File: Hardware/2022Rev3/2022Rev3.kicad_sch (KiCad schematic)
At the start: 88 parts, among them J1 Conn_01x04, J2 Conn_01x06, J3 RJ45_LED_Shielded, J4 Conn_01x09, J5 Conn_01x09, Q1 Q_NMOS_DGS, SW1 SW_SPDT, U1 ACS758xCB-200B-PFF, U10 PESD4USB3U-TBS, U11 PESD4USB3U-TBS, U2 LT1910, U3 TRS12433, U4 TRS12450, U5 Teensy4.1_DEV-16771, U6 Opamp_Dual, U7 Opamp_Dual, U8 Opamp_Dual, U9 Opamp_Dual

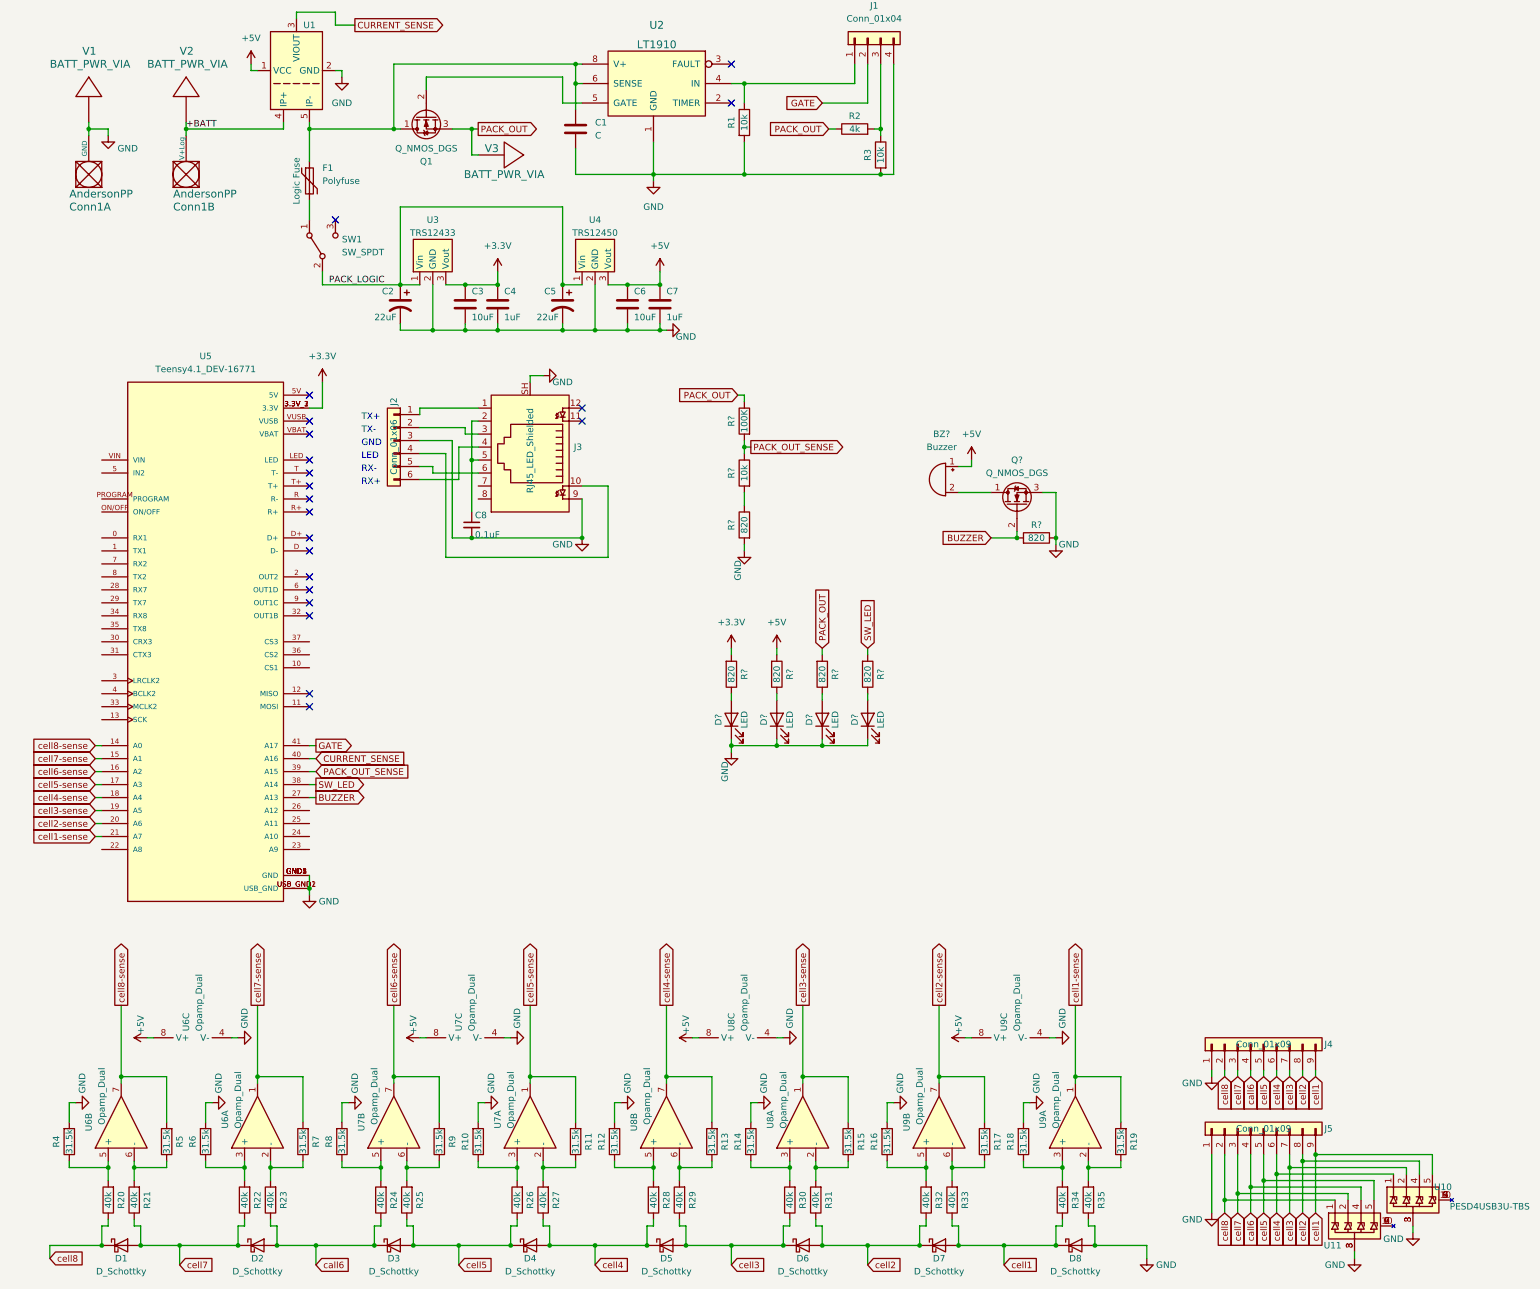
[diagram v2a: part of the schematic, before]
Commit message: BMS layout complete pending ethernet circuit and review
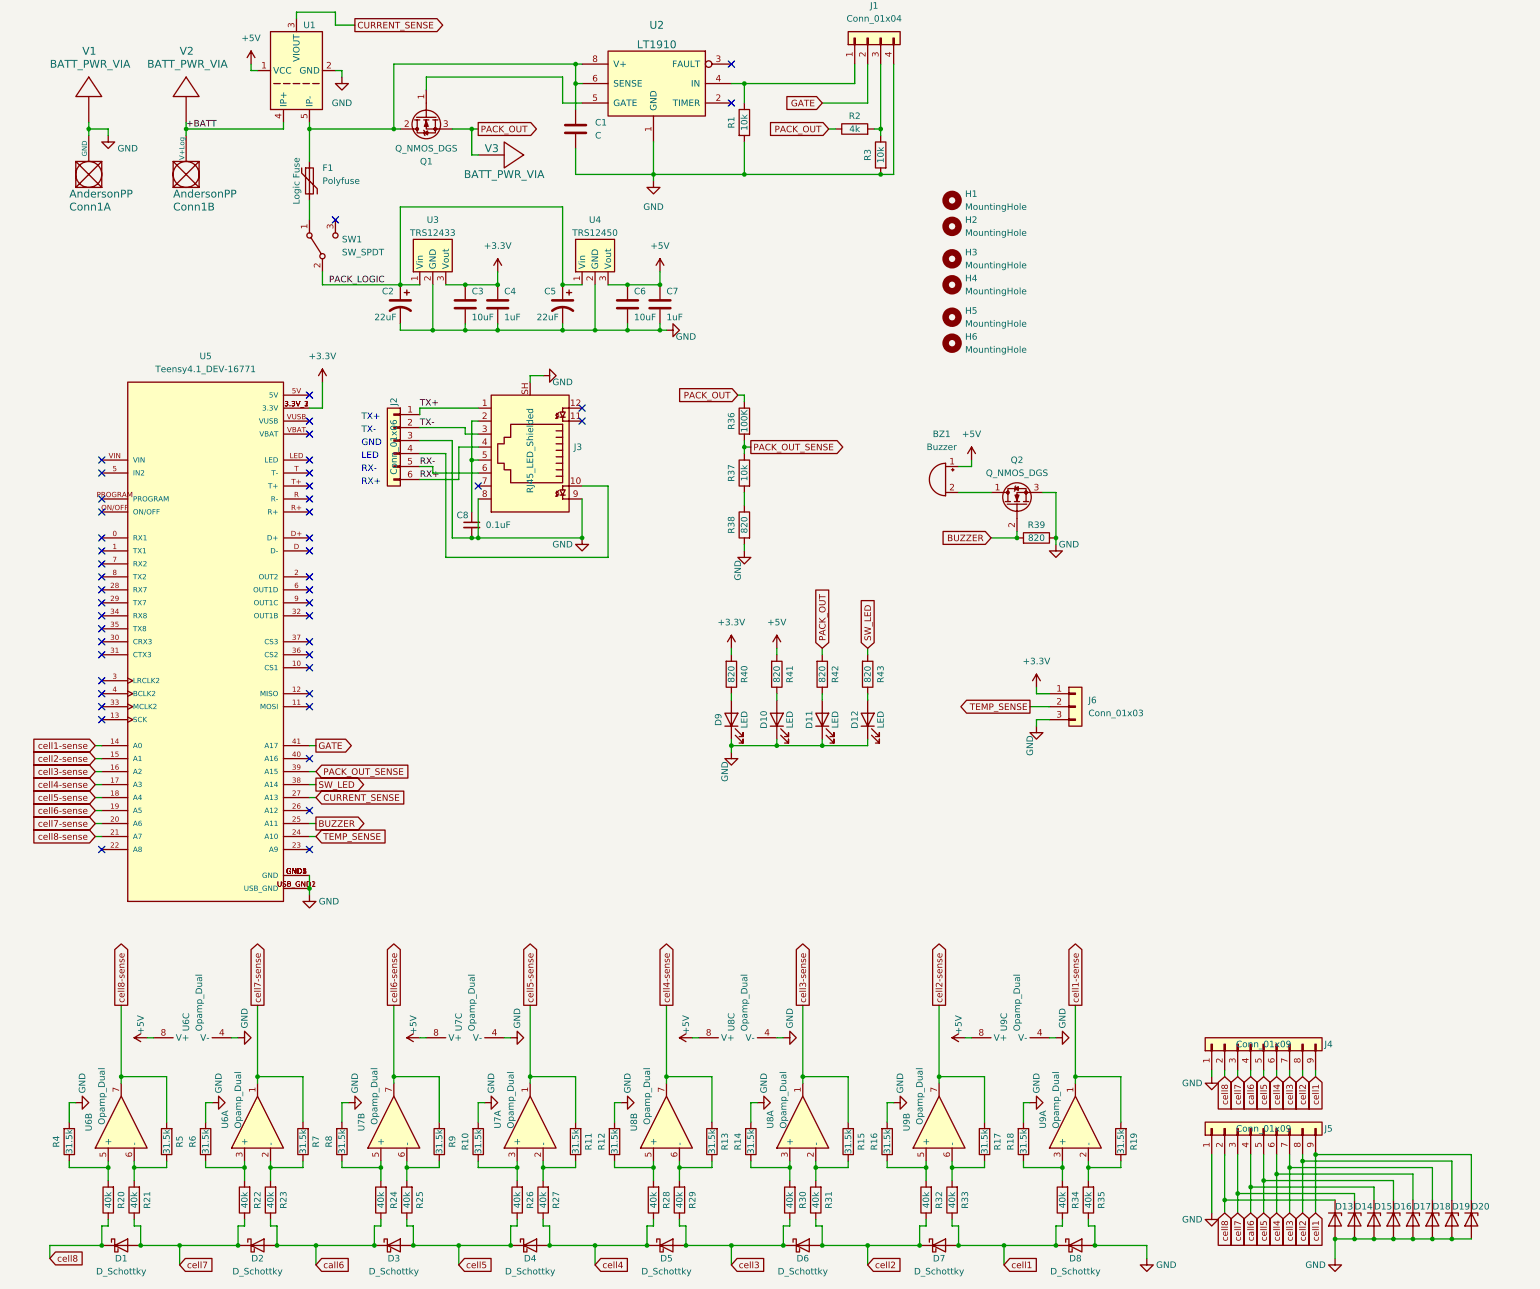
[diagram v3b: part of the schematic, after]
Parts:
- removed U10, U11: PESD4USB3U-TBS, symbol BMSRev3:PESD4USB3U-TBS
- added D13, D14, D15, D16, D17, D18, D19, D20: D_Zener, Diode_SMD:D_0603_1608Metric_Pad1.05x0.95mm_HandSolder, symbol Device:D_Zener
- added H1, H2, H3, H4: MountingHole, MRDT_Drill_Holes:4_40_Hole_Corner, symbol Mechanical:MountingHole
- added H5, H6: MountingHole, MRDT_Drill_Holes:4_40_Hole, symbol Mechanical:MountingHole
- added J6: Conn_01x03, MRDT_Connectors:MOLEX_SL_03_Vertical, symbol Connector_Generic:Conn_01x03
- BZ1: renamed from BZ?; footprint (none) -> MRDT_Devices:BUZZER_SMI_1324_TW_5V_2_R
- C1, C3, C4, C6, C7, C8: footprint (none) -> Capacitor_SMD:C_0603_1608Metric_Pad1.08x0.95mm_HandSolder
- C2, C5: footprint (none) -> Capacitor_THT:CP_Radial_D5.0mm_P2.50mm
- Conn1: footprint (none) -> MRDT_Connectors:Square_Anderson_2_V_Side_By_Side_PV
- D1, D2, D3, D4, D5, D6, D7, D8: footprint (none) -> Diode_SMD:D_0603_1608Metric_Pad1.05x0.95mm_HandSolder
- D10, D11, D12, D9: renamed from D?; footprint (none) -> LED_SMD:LED_0603_1608Metric_Pad1.05x0.95mm_HandSolder
- F1: footprint (none) -> Fuse:Fuse_2920_7451Metric_Pad2.10x5.45mm_HandSolder
- J1: footprint (none) -> MRDT_Connectors:MOLEX_SL_04_Vertical
- J2: footprint (none) -> Connector_PinHeader_2.00mm:PinHeader_2x03_P2.00mm_Vertical
- J3: footprint (none) -> MRDT_Connectors:RJ45_Teensy
- J4, J5: footprint (none) -> MRDT_Connectors:MOLEX_SL_09_Vertical
- Q1: footprint (none) -> MRDT_Actives:IRLS3034_TO-263-7_P; symbol Device:Q_NMOS_DGS -> Device:Q_NMOS_GDS
- Q2: renamed from Q?; footprint (none) -> Package_TO_SOT_SMD:SOT-23_Handsoldering
- R1, R10, R11, R12, R13, R14, R15, R16, R17, R18, R19, R2, R20, R21, R22, R23, R24, R25, R26, R27, R28, R29, R3, R30, R31, R32, R33, R34, R35, R4, R5, R6, R7, R8, R9: footprint (none) -> Resistor_SMD:R_0603_1608Metric_Pad0.98x0.95mm_HandSolder
- R36, R37, R38, R39, R40, R41, R42, R43: renamed from R?; footprint (none) -> Resistor_SMD:R_0603_1608Metric_Pad0.98x0.95mm_HandSolder
- SW1: footprint (none) -> MRDT_Connectors:MOLEX_SL_03_Horizontal
- U2, U6, U7, U8, U9: footprint (none) -> Package_SO:SO-8_3.9x4.9mm_P1.27mm
- U3, U4: footprint (none) -> MRDT_Devices:TSR_1-2433
- U5: footprint MODULE_DEV-16771 -> MRDT_Shields:MODULE_DEV-16771
- V1, V2, V3: footprint (none) -> MRDT_Drill_Holes:BATT_PWR_VIA
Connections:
- net +3V3: now also J6.1 (Pin_1)
- net BUZZER: now also U5.25 (A11); no longer U5.27 (A13)
- net CURRENT_SENSE: now also U5.27 (A13); no longer U5.40 (A16)
- net GND: now also J3.8, D13.2 (A), D14.2 (A), D15.2 (A), D16.2 (A), D17.2 (A), D18.2 (A), D19.2 (A), D20.2 (A), J6.3 (Pin_3)
- net call6: now also D15.1 (K)
- net cell1: now also D20.1 (K)
- net cell1-sense: now also U5.14 (A0); no longer U5.21 (A7)
- net cell2: now also D19.1 (K)
- net cell2-sense: now also U5.15 (A1); no longer U5.20 (A6)
- net cell3: now also D18.1 (K)
- net cell3-sense: now also U5.16 (A2); no longer U5.19 (A5)
- net cell4: now also D17.1 (K)
- net cell4-sense: now also U5.17 (A3); no longer U5.18 (A4)
- net cell5: now also D16.1 (K)
- net cell5-sense: now also U5.18 (A4); no longer U5.17 (A3)
- net cell6-sense: now also U5.19 (A5); no longer U5.16 (A2)
- net cell7: now also D14.1 (K)
- net cell7-sense: now also U5.20 (A6); no longer U5.15 (A1)
- net cell8: now also D13.1 (K)
- net cell8-sense: now also U5.21 (A7); no longer U5.14 (A0)
- net TEMP_SENSE: now reaches U5.24 (A10)
- net TEMP_SENSE: now also J6.2 (Pin_2)
- net TX+: now reaches J2.1 (Pin_1), J3.1
- net TX-: now reaches J2.2 (Pin_2), J3.3
- net RX-: now reaches J2.5 (Pin_5), J3.6
- net RX+: now reaches J2.6 (Pin_6), J3.4
- net at C1.1, F1.1, U1.5 (IP-)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: now also Q1.2 (D); no longer Q1.1 (D)
- net at U2.5 (GATE): now also Q1.1 (G); no longer Q1.2 (G)
- no-connect marks 21 -> 47

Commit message: layout changes
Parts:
- removed C8: 0.1uF, Capacitor_SMD:C_0603_1608Metric_Pad1.08x0.95mm_HandSolder, symbol Device:C_Small
- removed J2: Conn_01x06, Connector_PinHeader_2.00mm:PinHeader_2x03_P2.00mm_Vertical, symbol Connector_Generic:Conn_01x06
- removed J3: RJ45_LED_Shielded, MRDT_Connectors:RJ45_Teensy, symbol Connector:RJ45_LED_Shielded
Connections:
- no-connect marks 47 -> 44
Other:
- note removed: "GND"
- note removed: "LED"
- note removed: "RX+"
- note removed: "RX-"
- note removed: "TX+"
- note removed: "TX-"

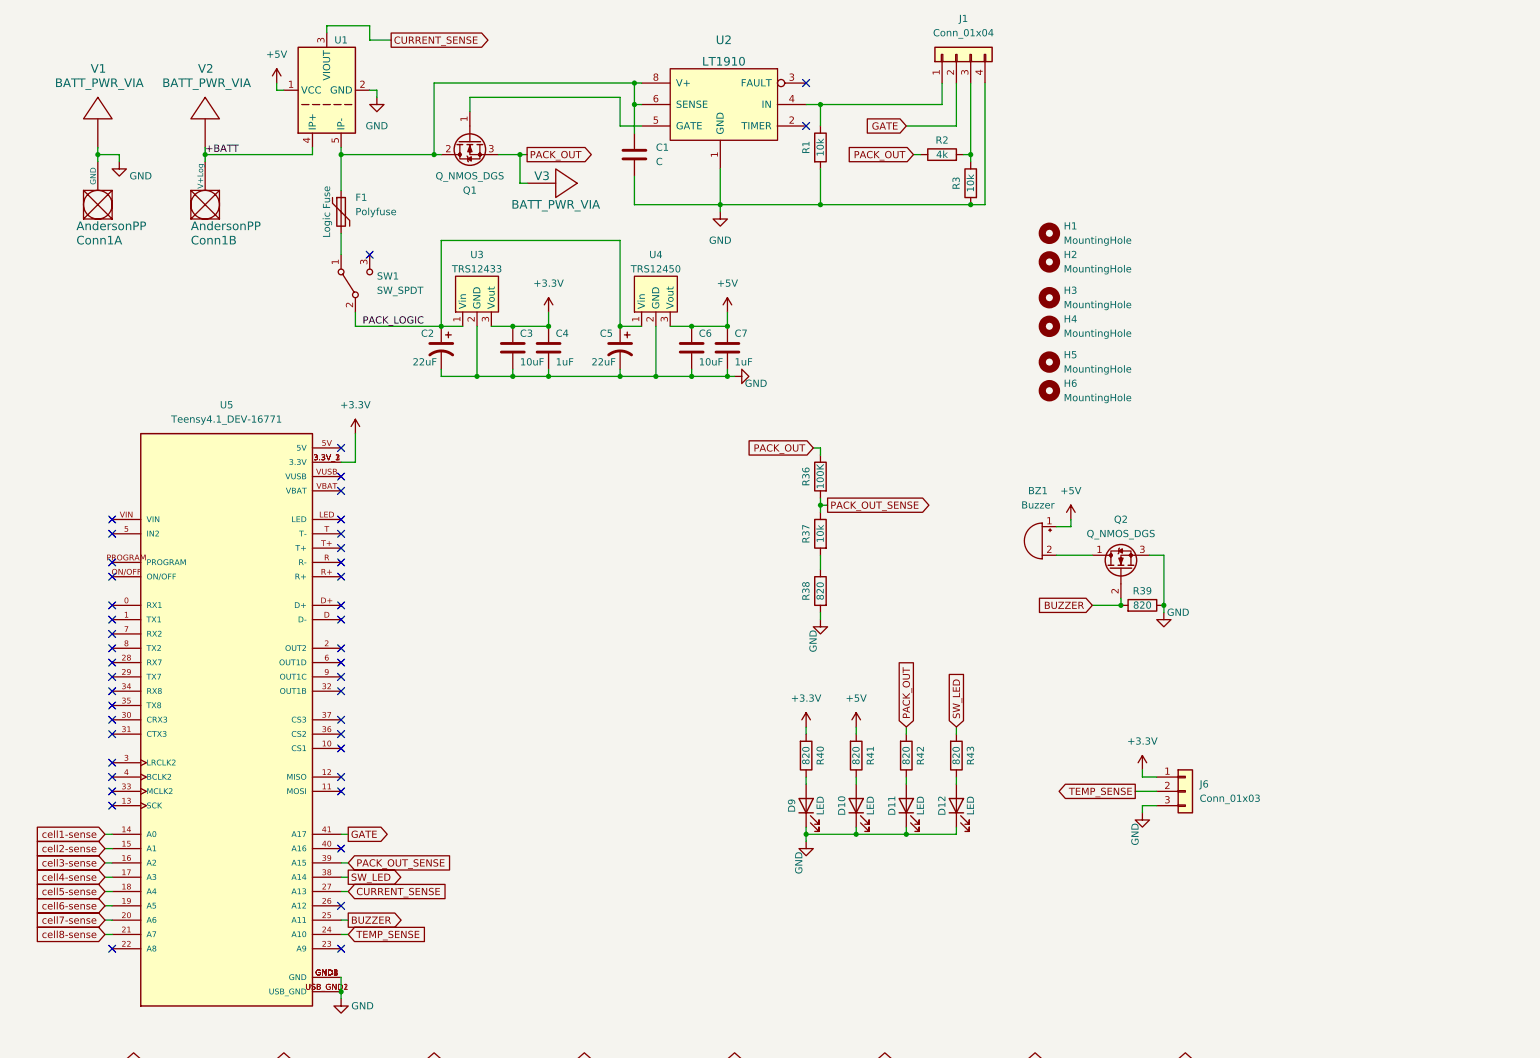
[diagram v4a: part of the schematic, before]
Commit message: Added fan circuit
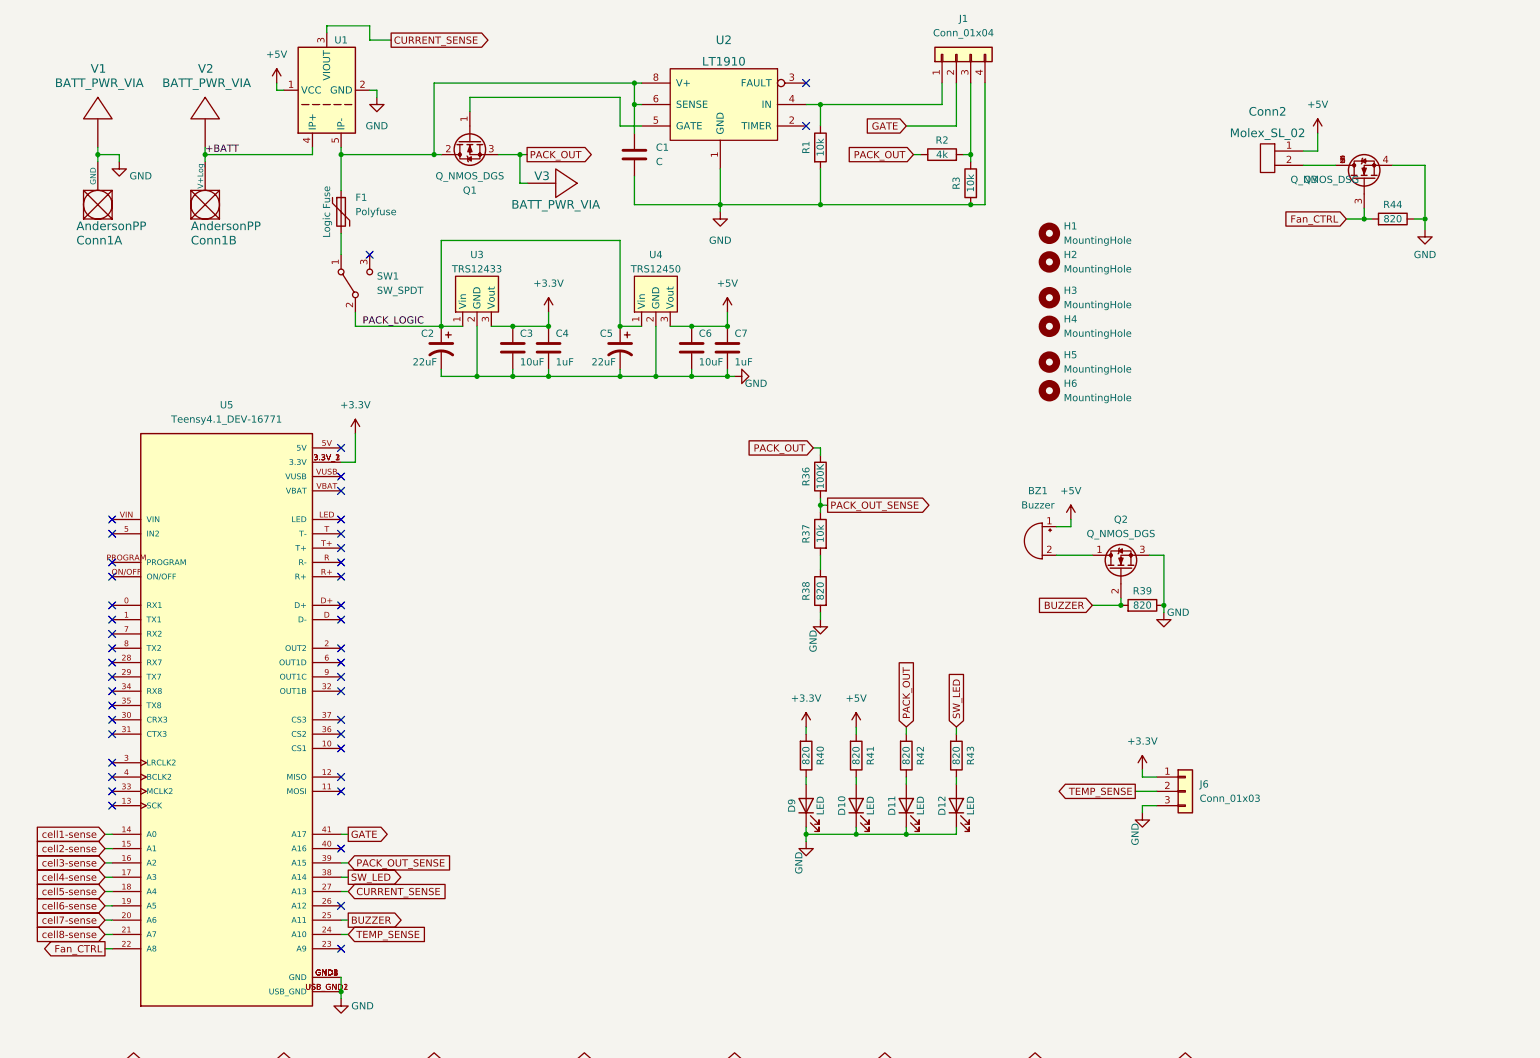
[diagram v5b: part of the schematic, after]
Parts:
- added Conn2: Molex_SL_02, MRDT_Connectors:MOLEX_SL_02_Vertical, symbol MRDT_Connectors:Molex_SL_02
- added Q3: Q_NMOS_DSG, Package_TO_SOT_SMD:SuperSOT-6, symbol Device:Q_NMOS_DSG
- added R44: 820, Resistor_SMD:R_0603_1608Metric_Pad0.98x0.95mm_HandSolder, symbol Device:R
- SW1: footprint MRDT_Connectors:MOLEX_SL_03_Horizontal -> MRDT_Connectors:MOLEX_SL_03_Vertical
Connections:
- net +5V: now also Conn2.1
- net GND: now also Q3.4 (S), R44.1
- net Fan_CTRL: now reaches U5.22 (A8)
- net Fan_CTRL: now also Q3.3 (G), R44.2
- new net: Conn2.2, Q3.1 (D), Q3.2 (D), Q3.5 (D), Q3.6 (D)
- no-connect marks 44 -> 43
